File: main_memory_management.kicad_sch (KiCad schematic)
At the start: 21 parts

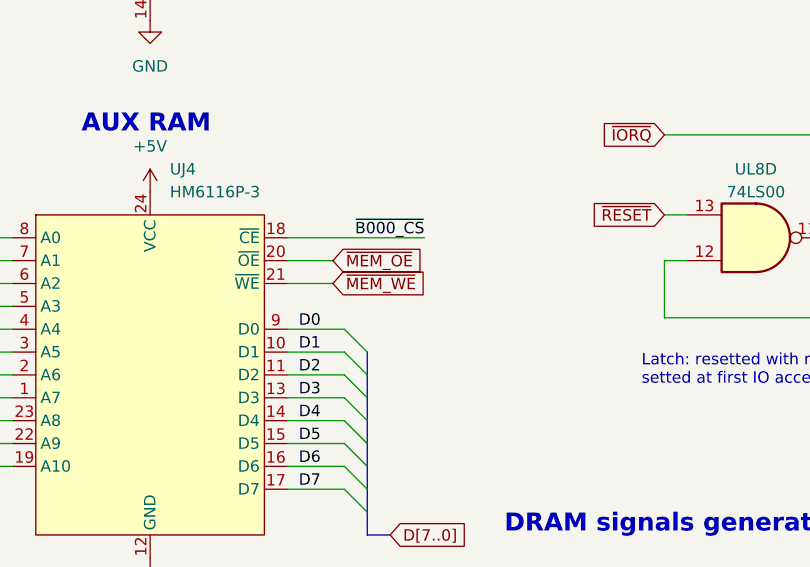
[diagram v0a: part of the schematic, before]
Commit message: Fixed wrong labels and connections, added footprint for dip switch
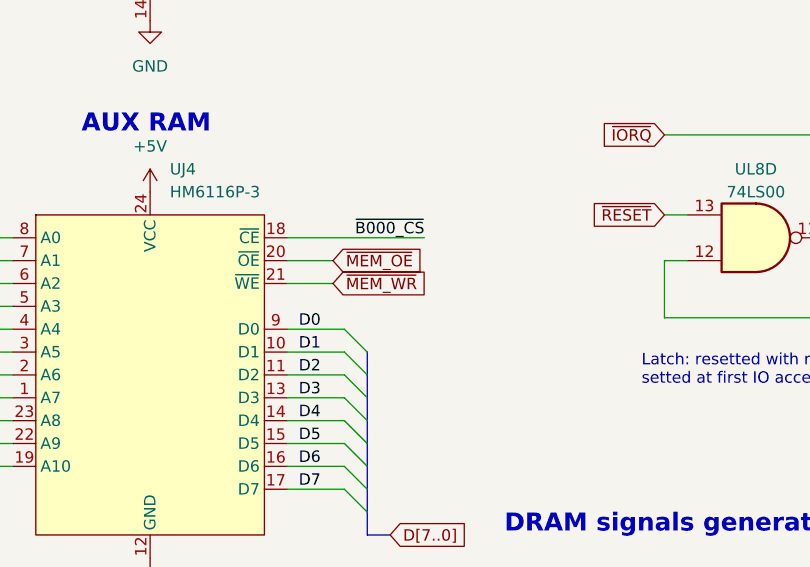
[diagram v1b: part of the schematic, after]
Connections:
- net ~{MEM_WE} renamed ~{MEM_WR}
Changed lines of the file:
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@@
 		)
 	)
-	(global_label "~{MEM_WE}"
+	(global_label "~{MEM_WR}"
 		(shape input)
 		(at 71.12 107.95 0)
@@
 		)
 		(property "Intersheetrefs" "${INTERSHEET_REFS}"
-			(at 81.725 107.95 0)
+			(at 81.846 107.95 0)
 			(effects
 				(font

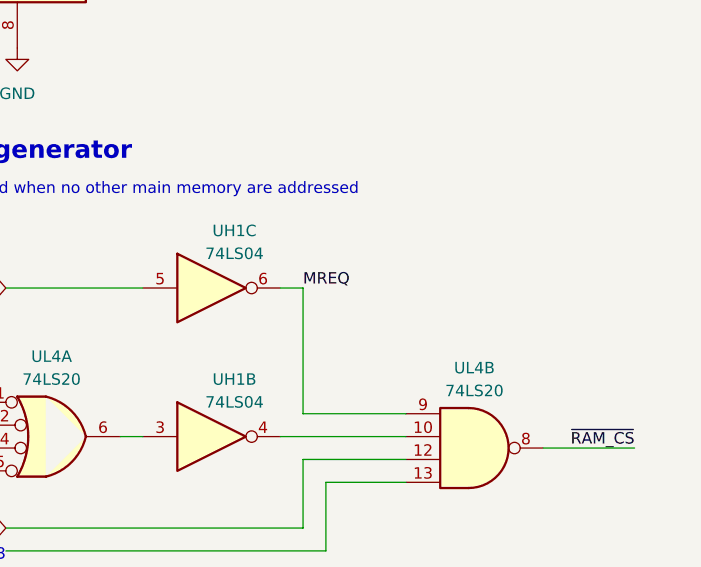
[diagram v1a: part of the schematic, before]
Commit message: Corrected MEM_OE and MREQ labels
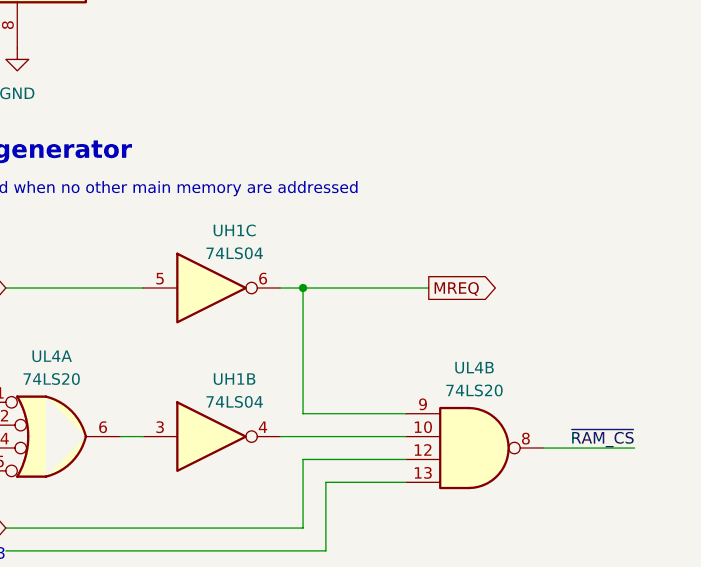
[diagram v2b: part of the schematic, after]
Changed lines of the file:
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@@
+	)
+	(junction
+		(at 246.38 85.09)
+		(diameter 0)
+		(color 0 0 0 0)
 	)
 	(junction
@@
 		)
 	)
+	(wire
+		(pts
+			(xy 246.38 85.09) (xy 260.35 85.09)
+		)
+		(stroke
+			(width 0)
+			(type default)
+		)
+	)
 	(bus
 		(pts
@@
 	(label "D7"
 		(at 67.31 130.81 0)
-		(effects
-			(font
-				(size 1.27 1.27)
-			)
-			(justify left bottom)
-		)
-	)
-	(label "MREQ"
-		(at 246.38 85.09 0)
 		(effects
 			(font
@@
 				(hide yes)
 			)
+		)
+	)
+	(global_label "MREQ"
+		(shape output)
+		(at 260.35 85.09 0)
+		(fields_autoplaced yes)
+		(effects
+			(font
+				(size 1.27 1.27)
+			)
+			(justify left)
+		)
+		(property "Intersheetrefs" "${INTERSHEET_REFS}"
+			(at 268.5361 85.09 0)
+			(effects
+				(font
+					(size 1.27 1.27)
+				)
+				(justify left)
+				(hide yes)
+			)

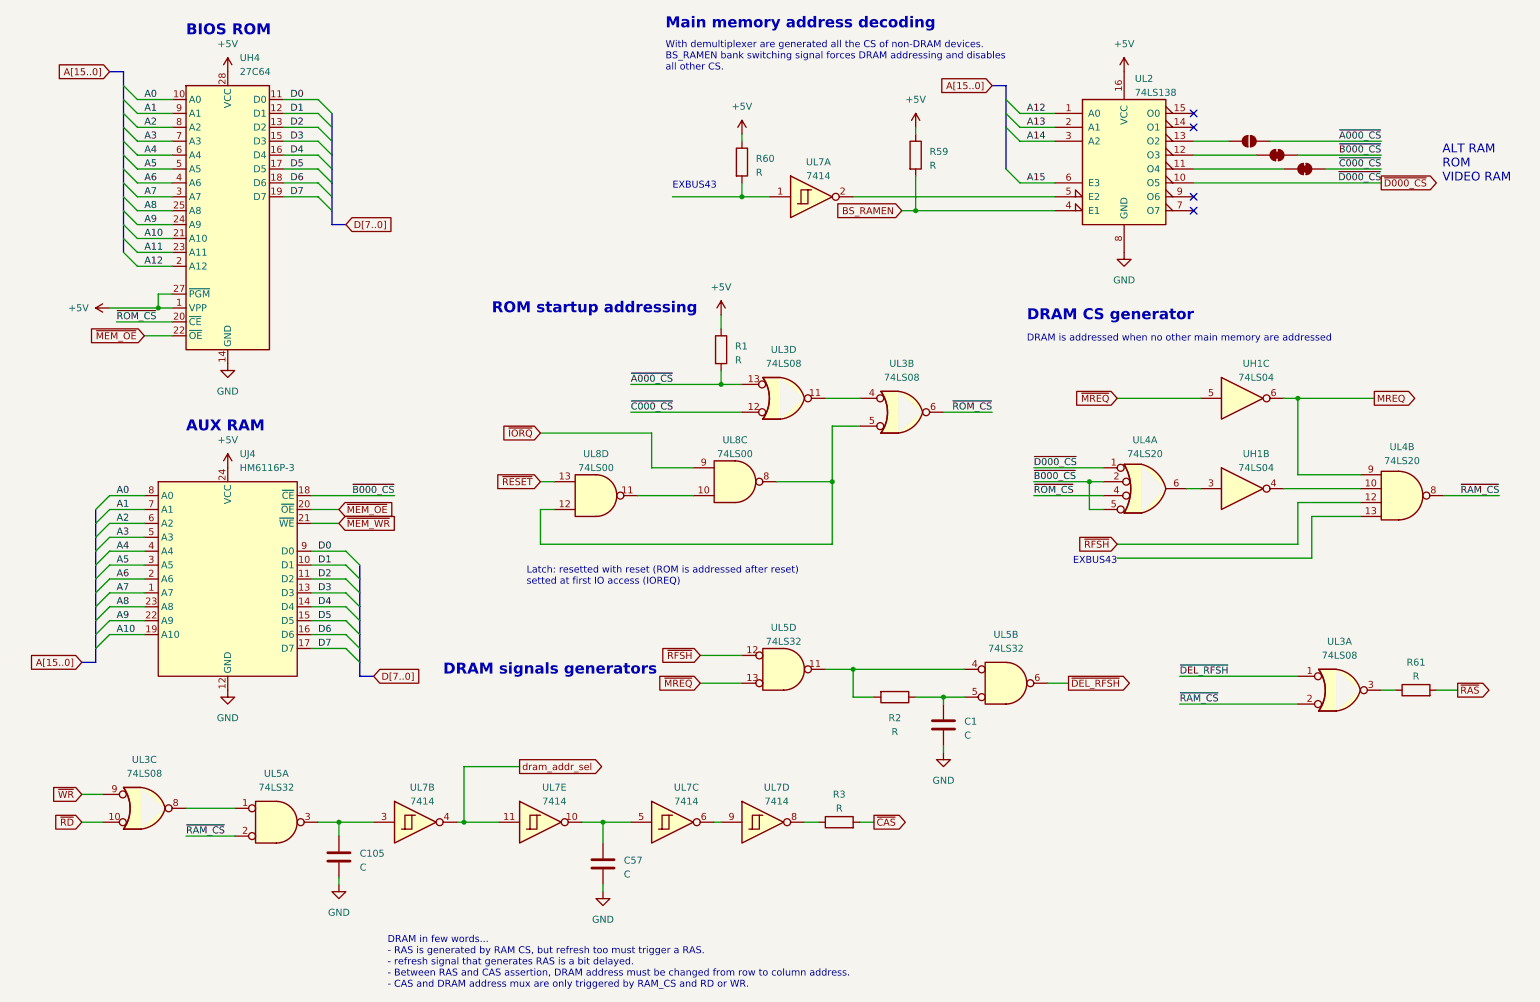
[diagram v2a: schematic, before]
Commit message: pcb: added and placed almost all components
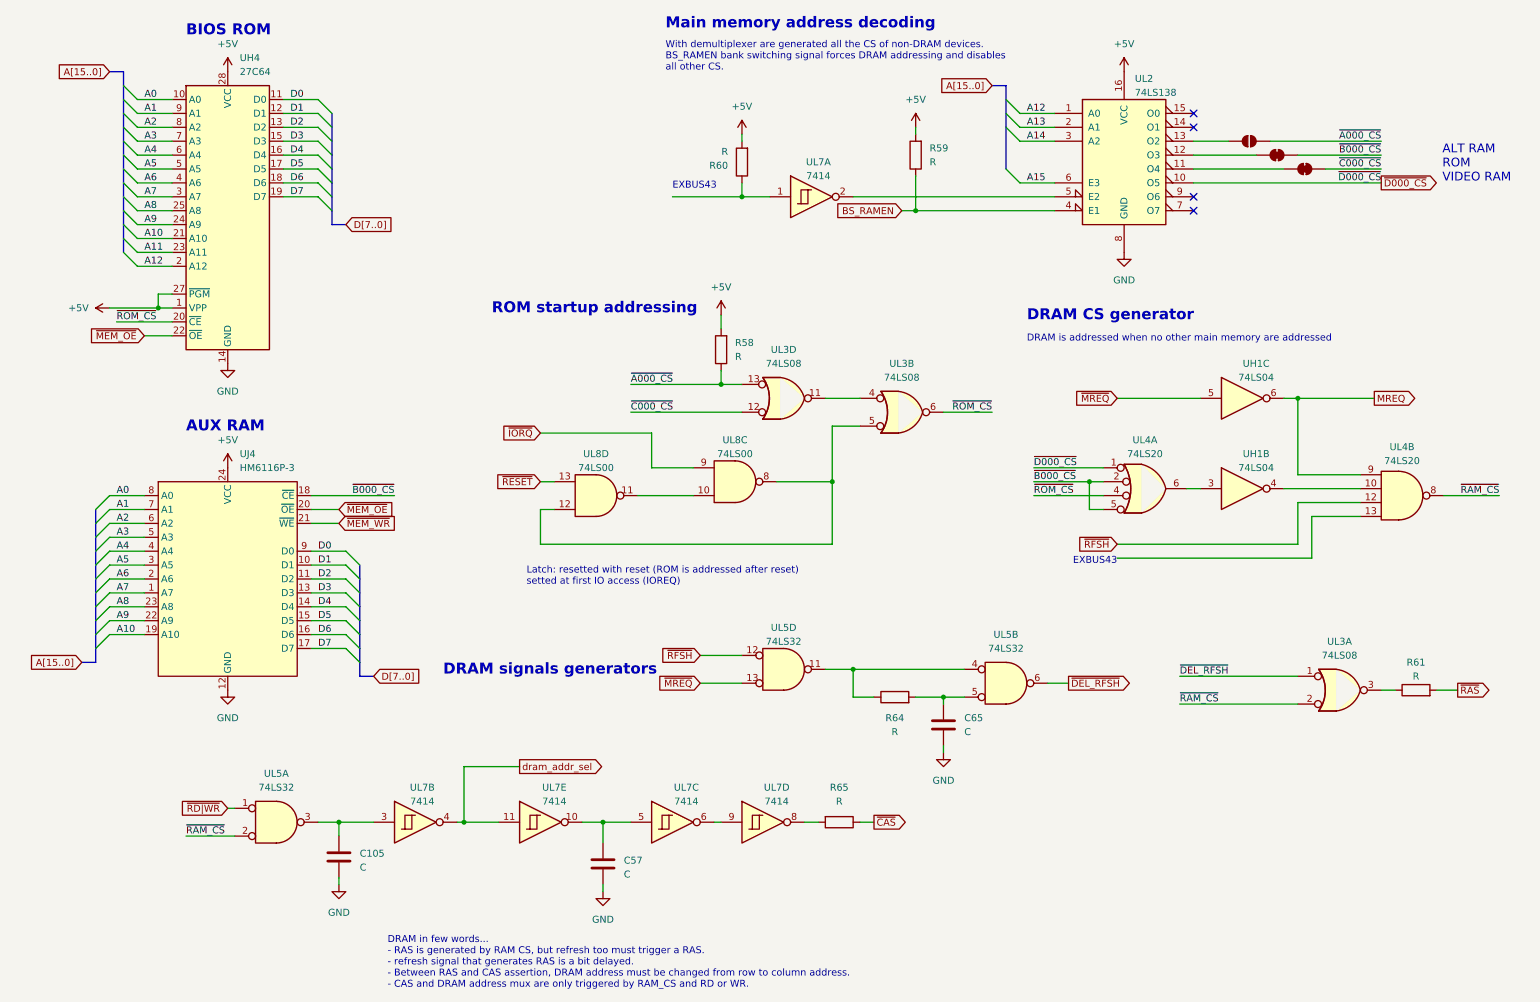
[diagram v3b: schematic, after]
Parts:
- removed unit 3 of UL3
- C105, C57: footprint (none) -> Capacitor_THT:C_Disc_D4.3mm_W1.9mm_P5.00mm
- C65: renamed from C1; footprint (none) -> Capacitor_THT:C_Disc_D4.3mm_W1.9mm_P5.00mm
- MAP1, MAP2, MAP3: footprint (none) -> Connector_PinHeader_2.54mm:PinHeader_2x01_P2.54mm_Vertical
- R58: renamed from R1; footprint (none) -> Resistor_THT:R_Axial_DIN0204_L3.6mm_D1.6mm_P5.08mm_Vertical
- R59, R60, R61: footprint (none) -> Resistor_THT:R_Axial_DIN0204_L3.6mm_D1.6mm_P5.08mm_Vertical
- R64: renamed from R2; footprint (none) -> Resistor_THT:R_Axial_DIN0204_L3.6mm_D1.6mm_P5.08mm_Vertical
- R65: renamed from R3; footprint (none) -> Resistor_THT:R_Axial_DIN0204_L3.6mm_D1.6mm_P5.08mm_Vertical
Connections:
- net +5V: now also R58.2, R59.2, R60.2; no longer R58.1, R59.1, R60.1
- net BS_RAMEN: now also R59.1; no longer R59.2
- net ~{A000_CS}: now also R58.1; no longer R58.2
- net ~{CAS}: now also R65.1; no longer R65.2
- net at UL5.11, UL5.4: now also R64.1; no longer R64.2
- net at C65.1, UL5.5: now also R64.2; no longer R64.1
- net ~{RD|WR}: now reaches UL5.1
- net at UL7.8: now also R65.2; no longer R65.1
- net at UL7.1: now also R60.1; no longer R60.2
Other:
- moved on the sheet: R58, R59, R60, R64, R65
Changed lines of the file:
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@@
 	(wire
 		(pts
-			(xy 24.13 162.56) (xy 27.94 162.56)
-		)
-		(stroke
-			(width 0)
-			(type default)
-		)
-	)
-	(wire
-		(pts
 			(xy 165.1 48.26) (xy 201.93 48.26)
 		)
@@
 	(wire
 		(pts
-			(xy 24.13 157.48) (xy 27.94 157.48)
-		)
-		(stroke
-			(width 0)
-			(type default)
-		)
-	)
-	(wire
-		(pts
 			(xy 34.29 45.72) (xy 40.64 45.72)
 		)
@@
 	(wire
 		(pts
-			(xy 43.18 160.02) (xy 52.07 160.02)
+			(xy 50.8 160.02) (xy 52.07 160.02)
 		)
 		(stroke
@@
 		)
 	)
-	(global_label "~{WR}"
-		(shape input)
-		(at 24.13 157.48 180)
-		(fields_autoplaced yes)
-		(effects
-			(font
-				(size 1.27 1.27)
-			)
-			(justify right)
-		)
-		(property "Intersheetrefs" "${INTERSHEET_REFS}"
-			(at 18.4234 157.48 0)
-			(effects
-				(font
-					(size 1.27 1.27)
-				)
-				(justify right)
-				(hide yes)
-			)
-		)
-	)
 	(global_label "~{RFSH}"
 		(shape input)
@@
 		)
 	)
-	(global_label "~{RAS}"
-		(shape output)
-		(at 275.59 138.43 0)
+	(global_label "~{RD|WR}"
+		(shape input)
+		(at 50.8 160.02 180)
 		(fields_autoplaced yes)
 		(effects
@@
 				(size 1.27 1.27)
 			)
-			(justify left)
+			(justify right)
 		)
 		(property "Intersheetrefs" "${INTERSHEET_REFS}"
-			(at 282.1433 138.43 0)
+			(at 41.3439 160.02 0)
 			(effects
 				(font
 					(size 1.27 1.27)
 				)
-				(justify left)
+				(justify right)
 				(hide yes)
 			)
 		)
 	)
-	(global_label "~{MREQ}"
-		(shape input)
-		(at 137.16 137.16 180)
+	(global_label "~{RAS}"
+		(shape output)
+		(at 275.59 138.43 0)
 		(fields_autoplaced yes)
 		(effects
@@
 				(size 1.27 1.27)
 			)
-			(justify right)
+			(justify left)
 		)
 		(property "Intersheetrefs" "${INTERSHEET_REFS}"
-			(at 128.9739 137.16 0)
+			(at 282.1433 138.43 0)
 			(effects
 				(font
 					(size 1.27 1.27)
 				)
-				(justify right)
+				(justify left)
 				(hide yes)
 			)
 		)
 	)
-	(global_label "~{RD}"
+	(global_label "~{MREQ}"
 		(shape input)
-		(at 24.13 162.56 180)
+		(at 137.16 137.16 180)
 		(fields_autoplaced yes)
 		(effects
@@
 		)
 		(property "Intersheetrefs" "${INTERSHEET_REFS}"
-			(at 18.6048 162.56 0)
+			(at 128.9739 137.16 0)
 			(effects
 				(font
@@
 			)
 		)
-		(property "Footprint" ""
+		(property "Footprint" "Capacitor_THT:C_Disc_D4.3mm_W1.9mm_P5.00mm"
 			(at 120.3452 173.99 0)
 			(effects
@@
 	(symbol
 		(lib_id "Device:R")
-		(at 176.53 40.64 0)
+		(at 176.53 40.64 180)
 		(unit 1)
 		(exclude_from_sim no)
@@
 		(fields_autoplaced yes)
 		(property "Reference" "R59"
-			(at 179.07 40.005 0)
+			(at 179.07 39.3699 0)
 			(effects
 				(font
 					(size 1.27 1.27)
 				)
-				(justify left)
+				(justify right)
 			)
 		)
 		(property "Value" "R"
-			(at 179.07 42.545 0)
+			(at 179.07 41.9099 0)
 			(effects
 				(font
 					(size 1.27 1.27)
 				)
-				(justify left)
+				(justify right)
 			)
 		)
-		(property "Footprint" ""
-			(at 174.752 40.64 90)
+		(property "Footprint" "Resistor_THT:R_Axial_DIN0204_L3.6mm_D1.6mm_P5.08mm_Vertical"
+			(at 178.308 40.64 90)
 			(effects
 				(font
@@
 	)
 	(symbol
-		(lib_id "74xx:74LS08")
-		(at 35.56 160.02 0)
-		(unit 3)
-		(convert 2)
-		(exclude_from_sim no)
-		(in_bom yes)
-		(on_board yes)
-		(dnp no)
-		(fields_autoplaced yes)
-		(property "Reference" "UL3"
-			(at 35.56 151.13 0)
-			(effects
-				(font
-					(size 1.27 1.27)
-				)
-			)
-		)
-		(property "Value" "74LS08"
-			(at 35.56 153.67 0)
-			(effects
-				(font
-					(size 1.27 1.27)
-				)
-			)
-		)
-		(property "Footprint" "Package_DIP:DIP-14_W7.62mm"
-			(at 35.56 160.02 0)
-			(effects
-				(font
-					(size 1.27 1.27)
-				)
-				(hide yes)
-			)
-		)
-		(property "Datasheet" "http://www.ti.com/lit/gpn/sn74LS08"
-			(at 35.56 160.02 0)
-			(effects
-				(font
-					(size 1.27 1.27)
-				)
-				(hide yes)
-			)
-		)
-		(property "Description" ""
-			(at 35.56 160.02 0)
-			(effects
-				(font
-					(size 1.27 1.27)
-				)
-			)
-		)
-		(pin "1"
-		)
-		(pin "2"
-		)
-		(pin "3"
-		)
-		(pin "4"
-		)
-		(pin "5"
-		)
-		(pin "6"
-		)
-		(pin "10"
-		)
-		(pin "8"
-		)
-		(pin "9"
-		)
-		(pin "11"
-		)
-		(pin "12"
-		)
-		(pin "13"
-		)
-		(pin "14"
-		)
-		(pin "7"
-		)
-		(instances
-			(project "ceda"
-				(path "/12a6dbe3-008d-4c5b-88f6-9f1c816060be/4fdb1b90-7ad1-4fa0-9b13-7b81abbda2ba"
-					(reference "UL3")
-					(unit 3)
-				)
-			)
-		)
-	)
-	(symbol
 		(lib_id "power:GND")
 		(at 71.12 173.99 0)
@@
 		(dnp no)
 		(fields_autoplaced yes)
-		(property "Reference" "C1"
-			(at 185.42 144.145 0)
+		(property "Reference" "C65"
+			(at 185.42 143.5099 0)
 			(effects
 				(font
@@
 		)
 		(property "Value" "C"
-			(at 185.42 146.685 0)
+			(at 185.42 146.0499 0)
 			(effects
 				(font
@@
 			)
 		)
-		(property "Footprint" ""
+		(property "Footprint" "Capacitor_THT:C_Disc_D4.3mm_W1.9mm_P5.00mm"
 			(at 182.5752 148.59 0)
 			(effects
@@
 			(project "ceda"
 				(path "/12a6dbe3-008d-4c5b-88f6-9f1c816060be/4fdb1b90-7ad1-4fa0-9b13-7b81abbda2ba"
-					(reference "C1")
+					(reference "C65")
 					(unit 1)
 				)
@@
 			)
 		)
-		(property "Footprint" ""
+		(property "Footprint" "Connector_PinHeader_2.54mm:PinHeader_2x01_P2.54mm_Vertical"
 			(at 237.49 38.1 0)
 			(effects
@@
 			)
 		)
-		(property "Footprint" ""
+		(property "Footprint" "Capacitor_THT:C_Disc_D4.3mm_W1.9mm_P5.00mm"
 			(at 72.0852 172.72 0)
 			(effects
@@
 	(symbol
 		(lib_id "Device:R")
-		(at 144.78 41.91 0)
+		(at 144.78 41.91 180)
 		(unit 1)
 		(exclude_from_sim no)
@@
 		(dnp no)
 		(property "Reference" "R60"
-			(at 147.32 41.275 0)
+			(at 142.24 42.545 0)
 			(effects
 				(font
@@
 		)
 		(property "Value" "R"
-			(at 147.32 43.815 0)
+			(at 142.24 40.005 0)
 			(effects
 				(font
@@
 			)
 		)
-		(property "Footprint" ""
-			(at 143.002 41.91 90)
+		(property "Footprint" "Resistor_THT:R_Axial_DIN0204_L3.6mm_D1.6mm_P5.08mm_Vertical"
+			(at 146.558 41.91 90)
 			(effects
 				(font
@@
 	(symbol
 		(lib_id "Device:R")
-		(at 140.97 76.2 0)
+		(at 140.97 76.2 180)
 		(unit 1)
 		(exclude_from_sim no)
@@
 		(dnp no)
 		(fields_autoplaced yes)
-		(property "Reference" "R1"
-			(at 143.51 75.565 0)
+		(property "Reference" "R58"
+			(at 143.51 74.9299 0)
 			(effects
 				(font
 					(size 1.27 1.27)
 				)
-				(justify left)
+				(justify right)
 			)
 		)
 		(property "Value" "R"
-			(at 143.51 78.105 0)
+			(at 143.51 77.4699 0)
 			(effects
 				(font
 					(size 1.27 1.27)
 				)
-				(justify left)
+				(justify right)
 			)
 		)
-		(property "Footprint" ""
-			(at 139.192 76.2 90)
+		(property "Footprint" "Resistor_THT:R_Axial_DIN0204_L3.6mm_D1.6mm_P5.08mm_Vertical"
+			(at 142.748 76.2 90)
 			(effects
 				(font
@@
 			(project "ceda"
 				(path "/12a6dbe3-008d-4c5b-88f6-9f1c816060be/4fdb1b90-7ad1-4fa0-9b13-7b81abbda2ba"
-					(reference "R1")
+					(reference "R58")
 					(unit 1)
 				)
@@
 			)
 		)
-		(property "Footprint" ""
+		(property "Footprint" "Connector_PinHeader_2.54mm:PinHeader_2x01_P2.54mm_Vertical"
 			(at 247.65 43.18 0)
 			(effects
@@
 			)
 		)
-		(property "Footprint" ""
+		(property "Footprint" "Connector_PinHeader_2.54mm:PinHeader_2x01_P2.54mm_Vertical"
 			(at 242.57 40.64 0)
 			(effects
@@
 			)
 		)
-		(property "Footprint" ""
+		(property "Footprint" "Resistor_THT:R_Axial_DIN0204_L3.6mm_D1.6mm_P5.08mm_Vertical"
 			(at 267.97 140.208 90)
 			(effects
@@
 	(symbol
 		(lib_id "Device:R")
-		(at 162.56 162.56 90)
+		(at 162.56 162.56 270)
 		(unit 1)
 		(exclude_from_sim no)
@@
 		(dnp no)
 		(fields_autoplaced yes)
-		(property "Reference" "R3"
-			(at 162.56 157.48 90)
+		(property "Reference" "R65"
+			(at 162.56 156.21 90)
 			(effects
 				(font
@@
 		)
 		(property "Value" "R"
-			(at 162.56 160.02 90)
+			(at 162.56 158.75 90)
 			(effects
 				(font
@@
 			)
 		)
-		(property "Footprint" ""
-			(at 162.56 164.338 90)
+		(property "Footprint" "Resistor_THT:R_Axial_DIN0204_L3.6mm_D1.6mm_P5.08mm_Vertical"
+			(at 162.56 160.782 90)
 			(effects
 				(font
@@
 			(project "ceda"
 				(path "/12a6dbe3-008d-4c5b-88f6-9f1c816060be/4fdb1b90-7ad1-4fa0-9b13-7b81abbda2ba"
-					(reference "R3")
+					(reference "R65")
 					(unit 1)
 				)
@@
 	(symbol
 		(lib_id "Device:R")
-		(at 172.72 139.7 270)
+		(at 172.72 139.7 90)
 		(unit 1)
 		(exclude_from_sim no)
@@
 		(dnp no)
 		(fields_autoplaced yes)
-		(property "Reference" "R2"
+		(property "Reference" "R64"
 			(at 172.72 143.51 90)
 			(effects
@@
 			)
 		)
-		(property "Footprint" ""
-			(at 172.72 137.922 90)
+		(property "Footprint" "Resistor_THT:R_Axial_DIN0204_L3.6mm_D1.6mm_P5.08mm_Vertical"
+			(at 172.72 141.478 90)
 			(effects
 				(font
@@
 			(project "ceda"
 				(path "/12a6dbe3-008d-4c5b-88f6-9f1c816060be/4fdb1b90-7ad1-4fa0-9b13-7b81abbda2ba"
-					(reference "R2")
+					(reference "R64")
 					(unit 1)
 				)
